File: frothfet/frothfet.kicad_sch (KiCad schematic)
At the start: 9 parts, among them U1 ESP32-S3-DEVKITC

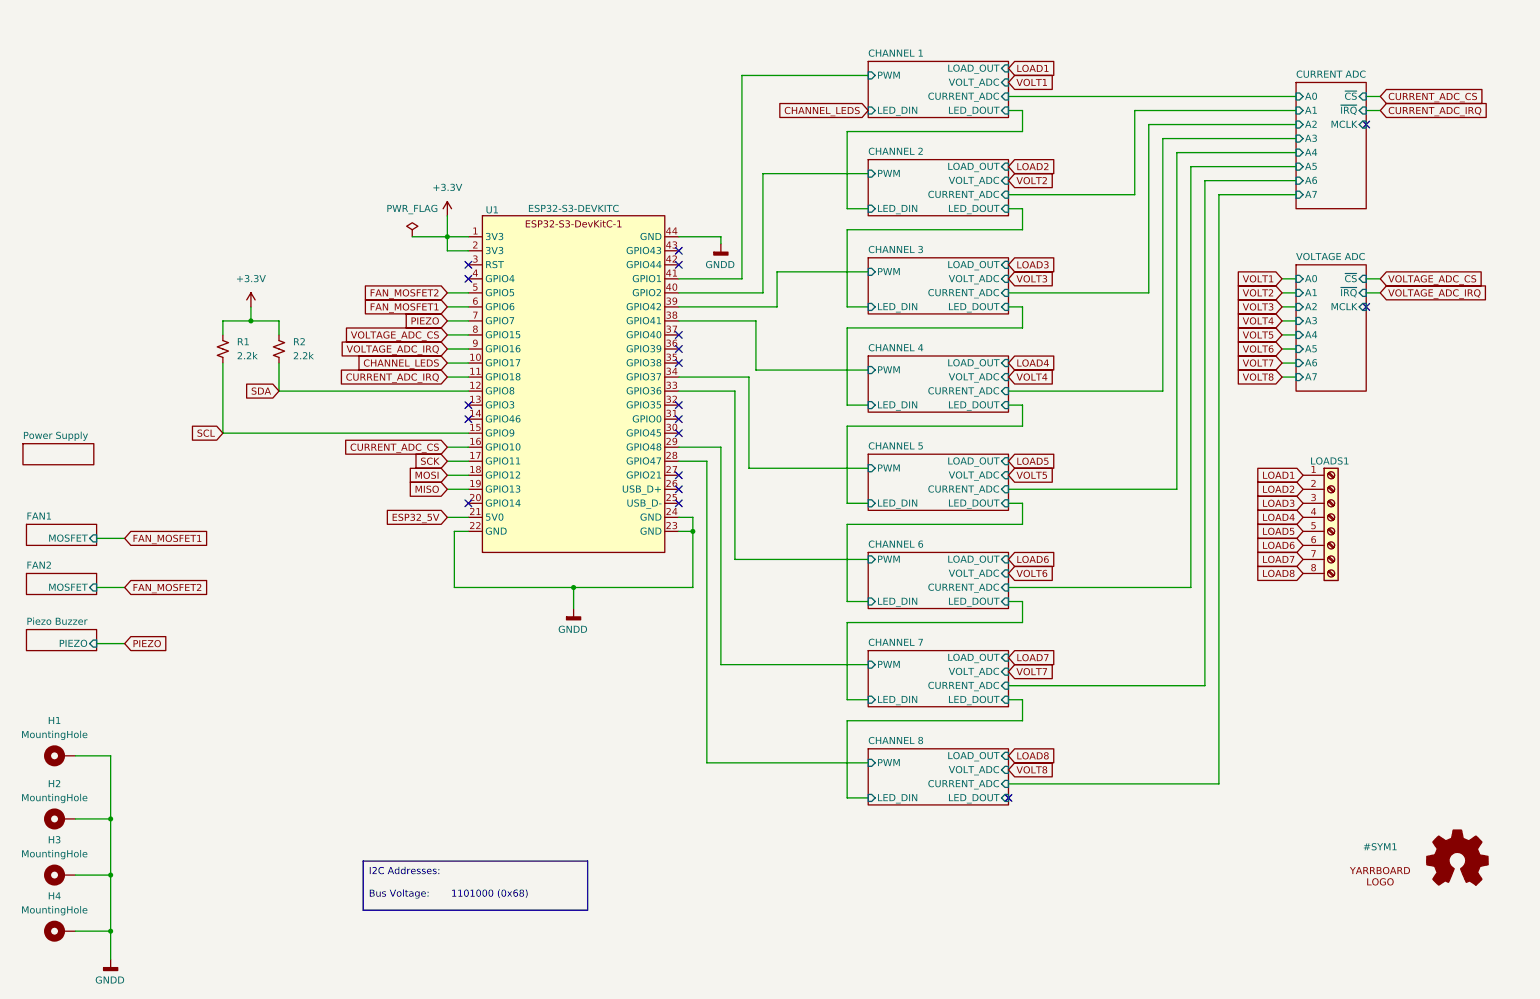
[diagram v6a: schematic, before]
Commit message: changed to 0603 and various tweaks
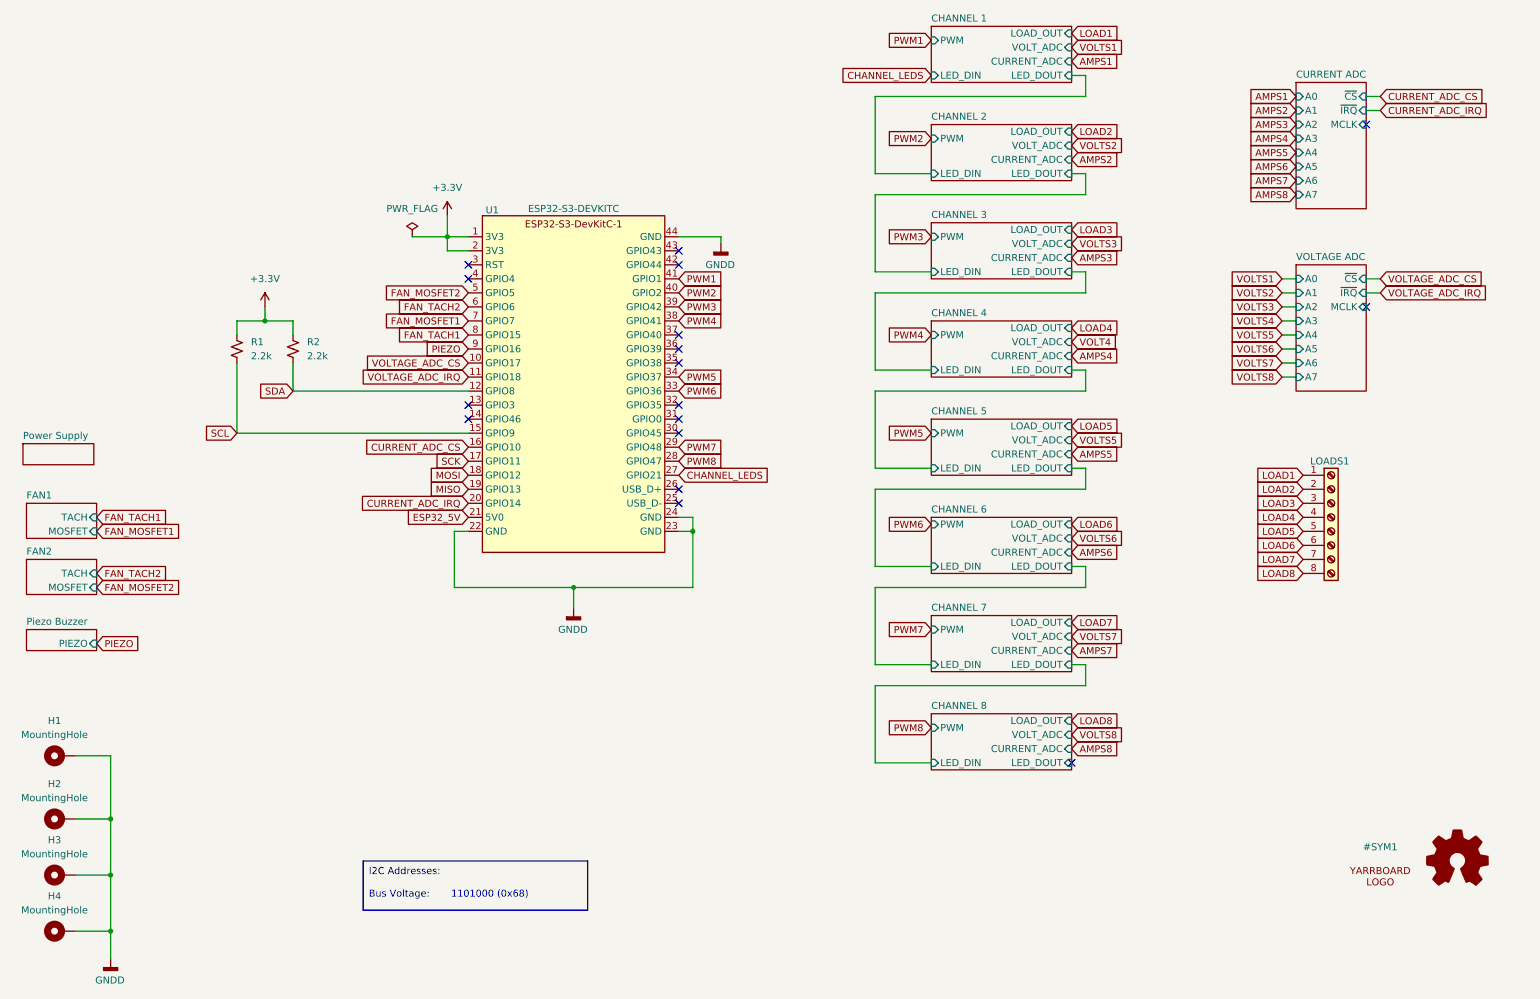
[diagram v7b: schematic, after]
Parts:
- R1, R2: footprint Resistor_SMD:R_0805_2012Metric_Pad1.20x1.40mm_HandSolder -> Resistor_SMD:R_0603_1608Metric
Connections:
- net CHANNEL_LEDS: now also U1.27 (GPIO21); no longer U1.10 (GPIO17)
- net CURRENT_ADC_IRQ: now also U1.20 (GPIO14); no longer U1.11 (GPIO18)
- net FAN_MOSFET1: now also U1.7 (GPIO7); no longer U1.6 (GPIO6)
- net PIEZO: now also U1.9 (GPIO16); no longer U1.7 (GPIO7)
- net VOLTAGE_ADC_CS: now also U1.10 (GPIO17); no longer U1.8 (GPIO15)
- net VOLTAGE_ADC_IRQ: now also U1.11 (GPIO18); no longer U1.9 (GPIO16)
- net CHANNEL 1/PWM renamed PWM1
- net CHANNEL 2/PWM renamed PWM2
- net CHANNEL 3/PWM renamed PWM3
- net CHANNEL 4/PWM renamed PWM4
- net CHANNEL 5/PWM renamed PWM5
- net CHANNEL 6/PWM renamed PWM6
- net CHANNEL 7/PWM renamed PWM7
- net CHANNEL 8/PWM renamed PWM8
- new net FAN_TACH1: U1.8 (GPIO15)
- new net FAN_TACH2: U1.6 (GPIO6)
- no-connect marks 19 -> 17
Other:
- sheet FAN1 ports: added TACH; removed none
- sheet FAN2 ports: added TACH; removed none
- moved on the sheet: R1, R2

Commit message: updated to kicad v9
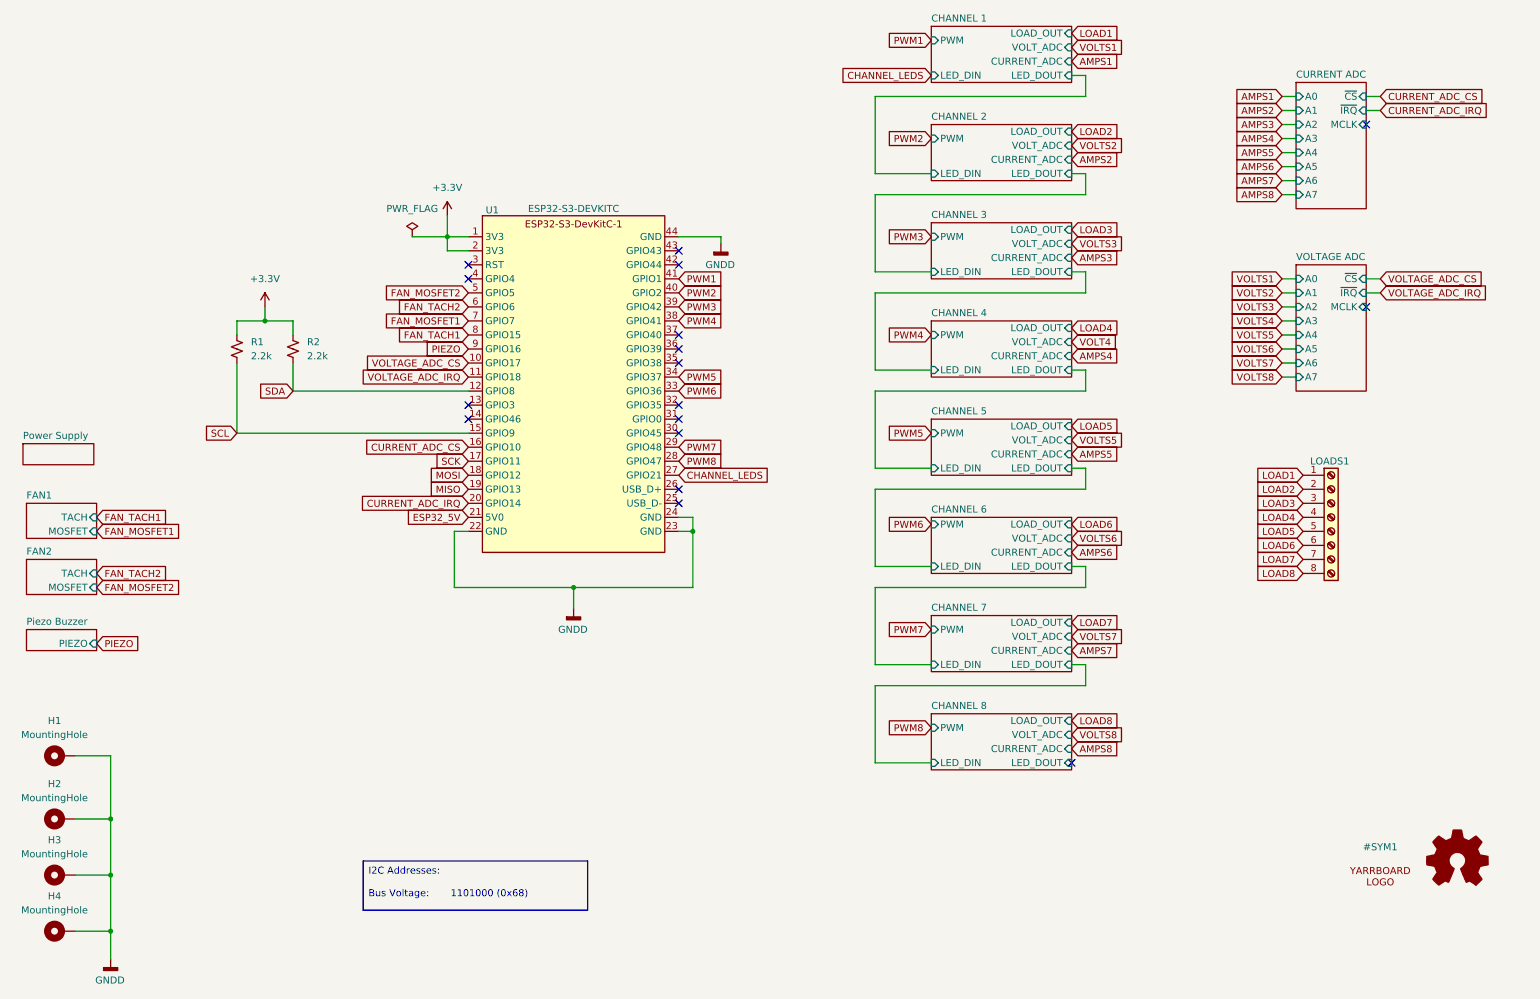
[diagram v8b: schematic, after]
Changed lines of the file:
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@@
 (kicad_sch
-	(version 20231120)
+	(version 20250114)
 	(generator "eeschema")
-	(generator_version "8.0")
+	(generator_version "9.0")
 	(paper "A4")
 	(title_block
@@
 		(company "https://github.com/hoeken/frothfet")
 	)
+	(text_box "I2C Addresses:\n\nBus Voltage:       1101000 (0x68)"
+		(exclude_from_sim no)
+		(at 77.47 173.99 0)
+		(size 40.64 8.89)
+		(margins 0.9525 0.9525 0.9525 0.9525)
+		(stroke
+			(width 0)
+			(type default)
+		)
+		(fill
+			(type none)
+		)
+		(effects
+			(font
+				(size 1.27 1.27)
+			)
+			(justify left top)
+		)
+	)
 	(junction
 		(at 115.57 124.46)
@@
 	(wire
 		(pts
+			(xy 243.84 48.26) (xy 246.38 48.26)
+		)
+		(stroke
+			(width 0)
+			(type default)
+		)
+	)
+	(wire
+		(pts
 			(xy 59.69 76.2) (xy 64.77 76.2)
 		)
@@
 	(wire
 		(pts
+			(xy 243.84 53.34) (xy 246.38 53.34)
+		)
+		(stroke
+			(width 0)
+			(type default)
+		)
+	)
+	(wire
+		(pts
 			(xy 170.18 49.53) (xy 180.34 49.53)
 		)
@@
 	(wire
 		(pts
+			(xy 243.84 45.72) (xy 246.38 45.72)
+		)
+		(stroke
+			(width 0)
+			(type default)
+		)
+	)
+	(wire
+		(pts
 			(xy 170.18 71.12) (xy 170.18 85.09)
 		)
@@
 	(wire
 		(pts
+			(xy 243.84 50.8) (xy 246.38 50.8)
+		)
+		(stroke
+			(width 0)
+			(type default)
+		)
+	)
+	(wire
+		(pts
 			(xy 170.18 120.65) (xy 180.34 120.65)
 		)
@@
 	(wire
 		(pts
+			(xy 243.84 40.64) (xy 246.38 40.64)
+		)
+		(stroke
+			(width 0)
+			(type default)
+		)
+	)
+	(wire
+		(pts
 			(xy 205.74 31.75) (xy 208.28 31.75)
 		)
@@
 	(wire
 		(pts
+			(xy 243.84 38.1) (xy 246.38 38.1)
+		)
+		(stroke
+			(width 0)
+			(type default)
+		)
+	)
+	(wire
+		(pts
+			(xy 243.84 35.56) (xy 246.38 35.56)
+		)
+		(stroke
+			(width 0)
+			(type default)
+		)
+	)
+	(wire
+		(pts
 			(xy 243.84 73.66) (xy 246.38 73.66)
 		)
@@
 	(wire
 		(pts
-			(xy 205.74 138.43) (xy 208.28 138.43)
+			(xy 243.84 43.18) (xy 246.38 43.18)
 		)
 		(stroke
@@
 	(wire
 		(pts
-			(xy 170.18 67.31) (xy 180.34 67.31)
+			(xy 205.74 138.43) (xy 208.28 138.43)
 		)
 		(stroke
@@
 		)
 	)
-	(text_box "I2C Addresses:\n\nBus Voltage:       1101000 (0x68)"
-		(exclude_from_sim no)
-		(at 77.47 173.99 0)
-		(size 40.64 8.89)
+	(wire
+		(pts
+			(xy 170.18 67.31) (xy 180.34 67.31)
+		)
 		(stroke
 			(width 0)
 			(type default)
 		)
-		(fill
-			(type none)
-		)
-		(effects
-			(font
-				(size 1.27 1.27)
-			)
-			(justify left top)
-		)
 	)
 	(global_label "AMPS7"
@@
 	(global_label "AMPS8"
 		(shape input)
-		(at 246.38 53.34 180)
+		(at 243.84 53.34 180)
 		(fields_autoplaced yes)
 		(effects
@@
 		)
 		(property "Intersheetrefs" "${INTERSHEET_REFS}"
-			(at 237.1658 53.34 0)
+			(at 234.6258 53.34 0)
 			(effects
 				(font
@@
 	(global_label "AMPS6"
 		(shape input)
-		(at 246.38 48.26 180)
+		(at 243.84 48.26 180)
 		(fields_autoplaced yes)
 		(effects
@@
 		)
 		(property "Intersheetrefs" "${INTERSHEET_REFS}"
-			(at 237.1658 48.26 0)
+			(at 234.6258 48.26 0)
 			(effects
 				(font
@@
 	(global_label "AMPS2"
 		(shape input)
-		(at 246.38 38.1 180)
+		(at 243.84 38.1 180)
 		(fields_autoplaced yes)
 		(effects
@@
 		)
 		(property "Intersheetrefs" "${INTERSHEET_REFS}"
-			(at 237.1658 38.1 0)
+			(at 234.6258 38.1 0)
 			(effects
 				(font
@@
 	(global_label "AMPS1"
 		(shape input)
-		(at 246.38 35.56 180)
+		(at 243.84 35.56 180)
 		(fields_autoplaced yes)
 		(effects
@@
 		)
 		(property "Intersheetrefs" "${INTERSHEET_REFS}"
-			(at 237.1658 35.56 0)
+			(at 234.6258 35.56 0)
 			(effects
 				(font
@@
 	(global_label "AMPS4"
 		(shape input)
-		(at 246.38 43.18 180)
+		(at 243.84 43.18 180)
 		(fields_autoplaced yes)
 		(effects
@@
 		)
 		(property "Intersheetrefs" "${INTERSHEET_REFS}"
-			(at 237.1658 43.18 0)
+			(at 234.6258 43.18 0)
 			(effects
 				(font
@@
 	(global_label "AMPS5"
 		(shape input)
-		(at 246.38 45.72 180)
+		(at 243.84 45.72 180)
 		(fields_autoplaced yes)
 		(effects
@@
 		)
 		(property "Intersheetrefs" "${INTERSHEET_REFS}"
-			(at 237.1658 45.72 0)
+			(at 234.6258 45.72 0)
 			(effects
 				(font
@@
 	(global_label "AMPS7"
 		(shape input)
-		(at 246.38 50.8 180)
+		(at 243.84 50.8 180)
 		(fields_autoplaced yes)
 		(effects
@@
 		)
 		(property "Intersheetrefs" "${INTERSHEET_REFS}"
-			(at 237.1658 50.8 0)
+			(at 234.6258 50.8 0)
 			(effects
 				(font
@@
 	(global_label "AMPS3"
 		(shape input)
-		(at 246.38 40.64 180)
+		(at 243.84 40.64 180)
 		(fields_autoplaced yes)
 		(effects
@@
 		)
 		(property "Intersheetrefs" "${INTERSHEET_REFS}"
-			(at 237.1658 40.64 0)
+			(at 234.6258 40.64 0)
 			(effects
 				(font
@@
 		(at 16.51 119.38)
 		(size 12.7 6.35)
+		(exclude_from_sim no)
+		(in_bom yes)
+		(on_board yes)
+		(dnp no)
 		(fields_autoplaced yes)
 		(stroke
@@
 		(at 180.34 22.86)
 		(size 25.4 10.16)
+		(exclude_from_sim no)
+		(in_bom yes)
+		(on_board yes)
+		(dnp no)
 		(fields_autoplaced yes)
 		(stroke
@@
 		(at 16.51 132.08)
 		(size 12.7 3.81)
+		(exclude_from_sim no)
+		(in_bom yes)
+		(on_board yes)
+		(dnp no)
 		(fields_autoplaced yes)
 		(stroke
@@
 		(at 180.34 58.42)
 		(size 25.4 10.16)
+		(exclude_from_sim no)
+		(in_bom yes)
+		(on_board yes)
+		(dnp no)
 		(fields_autoplaced yes)
 		(stroke
@@
 		(at 180.34 111.76)
 		(size 25.4 10.16)
+		(exclude_from_sim no)
+		(in_bom yes)
+		(on_board yes)
+		(dnp no)
 		(fields_autoplaced yes)
 		(stroke
@@
 		(at 180.34 129.54)
 		(size 25.4 10.16)
+		(exclude_from_sim no)
+		(in_bom yes)
+		(on_board yes)
+		(dnp no)
 		(fields_autoplaced yes)
 		(stroke
@@
 		(at 180.34 76.2)
 		(size 25.4 10.16)
+		(exclude_from_sim no)
+		(in_bom yes)
+		(on_board yes)
+		(dnp no)
 		(fields_autoplaced yes)
 		(stroke
@@
 		(at 246.38 66.04)
 		(size 12.7 22.86)
+		(exclude_from_sim no)
+		(in_bom yes)
+		(on_board yes)
+		(dnp no)
 		(fields_autoplaced yes)
 		(stroke
@@
 		(at 180.34 93.98)
 		(size 25.4 10.16)
+		(exclude_from_sim no)
+		(in_bom yes)
+		(on_board yes)
+		(dnp no)
 		(fields_autoplaced yes)
 		(stroke
@@
 		(at 180.34 147.32)
 		(size 25.4 10.16)
+		(exclude_from_sim no)
+		(in_bom yes)
+		(on_board yes)
+		(dnp no)
 		(fields_autoplaced yes)
 		(stroke
@@
 		(at 16.51 109.22)
 		(size 12.7 6.35)
+		(exclude_from_sim no)
+		(in_bom yes)
+		(on_board yes)
+		(dnp no)
 		(fields_autoplaced yes)
 		(stroke
@@
 		(at 246.38 33.02)
 		(size 12.7 22.86)
+		(exclude_from_sim no)
+		(in_bom yes)
+		(on_board yes)
+		(dnp no)
 		(fields_autoplaced yes)
 		(stroke
@@
 		(at 180.34 40.64)
 		(size 25.4 10.16)
+		(exclude_from_sim no)
+		(in_bom yes)
+		(on_board yes)
+		(dnp no)
 		(fields_autoplaced yes)
 		(stroke
@@
 		(at 15.875 98.425)
 		(size 12.827 3.81)
+		(exclude_from_sim no)
+		(in_bom yes)
+		(on_board yes)
+		(dnp no)
 		(fields_autoplaced yes)
 		(stroke
@@
 		)
 	)
+	(embedded_fonts no)
 )
